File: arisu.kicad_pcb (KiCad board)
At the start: 2 copper layers, 339.1 x 118.7 mm, 166 parts, among them J1 USB_B_Micro, J10 PF6, J11 PF7, J12 VCC, J13 D+, J14 D-, J15 GND, J2 MISO, J3 VCC, J4 SCK, J5 MOSI, J6 RES, J7 GND, J8 PF4, J9 PF5, SW1 SW_Push, SW10 SW_Push, SW11 SW_Push, SW12 SW_Push, SW13 SW_Push, SW14 SW_Push, SW15 SW_Push, SW16 SW_Push, SW17 SW_Push, SW18 SW_Push, SW19 SW_Push, SW2 SW_Push, SW20 SW_Push, SW21 SW_Push, SW22 SW_Push, SW23 SW_Push, SW24 SW_Push, SW25 SW_Push, SW26 SW_Push, SW27 SW_Push, SW28 SW_Push, SW29 SW_Push, SW3 SW_Push, SW30 SW_Push, SW31 SW_Push, SW32 SW_Push, SW33 SW_Push, SW34 SW_Push, SW35 SW_Push, SW36 SW_Push, SW37 SW_Push, SW38 SW_Push, SW39 SW_Push, SW4 SW_Push, SW40 SW_Push, SW41 SW_Push, SW42 SW_Push, SW43 SW_Push, SW44 SW_Push, SW45 SW_Push, SW46 SW_Push, SW47 SW_Push, SW48 SW_Push, SW49 SW_Push, SW5 SW_Push, SW50 SW_Push, SW51 SW_Push, SW52 SW_Push, SW53 SW_Push, SW54 SW_Push, SW55 SW_Push, SW56 SW_Push, SW57 SW_Push, SW58 SW_Push, SW59 SW_Push, SW6 SW_Push, SW60 SW_Push, SW61 SW_Push, SW62 SW_Push, SW63 SW_Push, SW64 SW_Push, SW65 SW_Push, SW66 SW_Push, SW67 SW_Push, SW7 SW_Push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

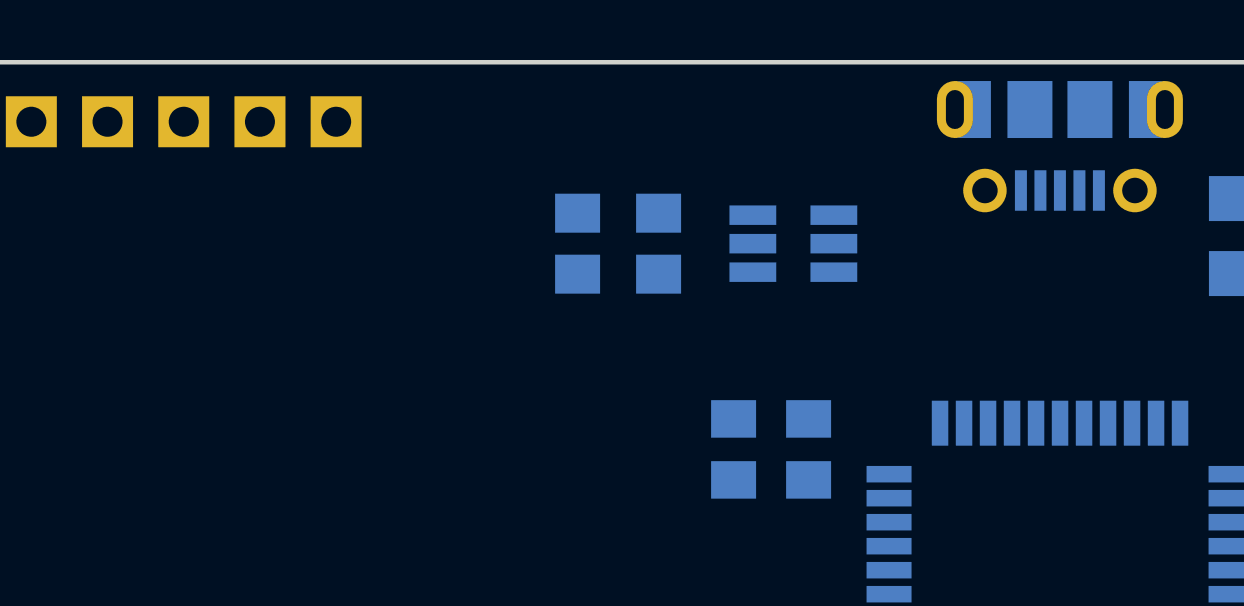
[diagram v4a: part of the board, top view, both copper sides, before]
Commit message: Route differential pair D+/D- pins to MCU
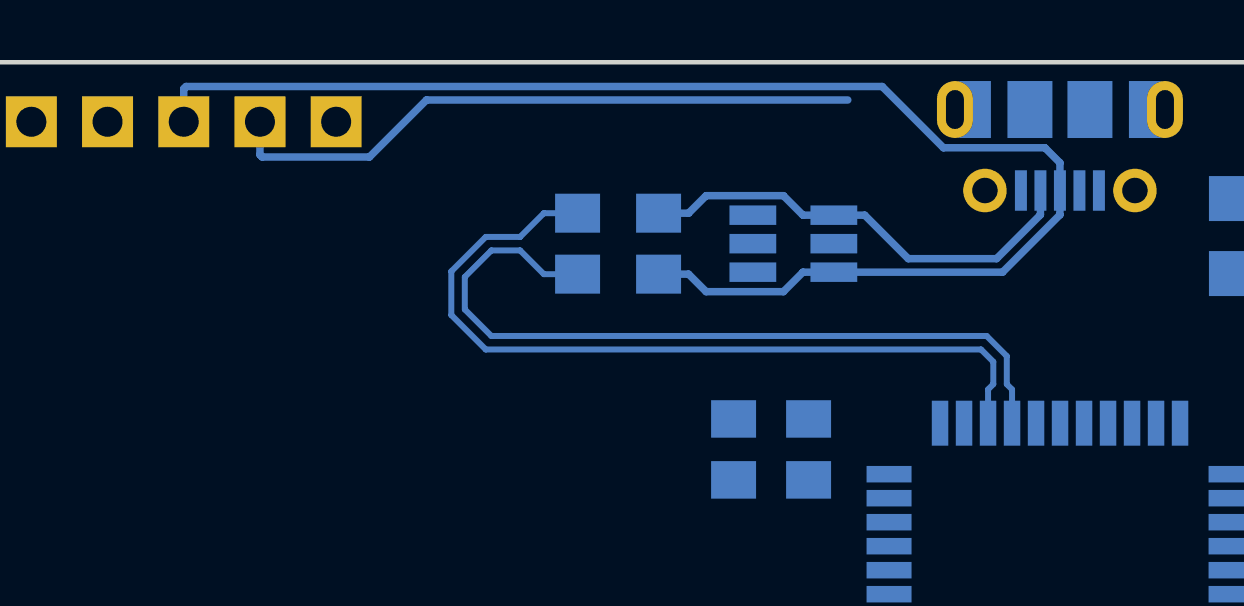
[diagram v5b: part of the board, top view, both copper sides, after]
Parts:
- moved R1 2.03 mm to (160.8, 31.5)
- moved R2 2.03 mm to (160.8, 29.5)
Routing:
- net Net-(J1-Pad3): track 0.00 -> 47.8 mm
- net Net-(J1-Pad2): track 0.00 -> 36.8 mm
- net D-: track 0.00 -> 27.3 mm
- net D+: track 0.00 -> 26.6 mm
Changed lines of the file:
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@@
     (thickness 1.6)
     (drawings 1380)
-    (tracks 0)
+    (tracks 52)
     (zones 0)
     (modules 166)
@@
   )
   (module Resistors_SMD:R_0805_HandSoldering (layer B.Cu)
-    (at 160.782 29.464)
+    (at 160.782 31.496)
     (descr "Resistor SMD 0805, hand soldering")
     (tags "resistor 0805")
@@
   )
   (module Resistors_SMD:R_0805_HandSoldering (layer B.Cu)
-    (at 160.782 31.496)
+    (at 160.782 29.464)
     (descr "Resistor SMD 0805, hand soldering")
     (tags "resistor 0805")
@@
   (gr_line (start 40.34 32.02) (end 40.64 31.72) (layer Eco2.User) (width 0.2))
   (gr_line (start 40.64 45.72) (end 40.34 45.42) (layer Eco2.User) (width 0.2))
+  (segment (start 175.509855 29.518002) (end 175.509855 28.708) (width 0.25) (layer B.Cu) (net 78))
+  (segment (start 167.974 31.43) (end 173.597857 31.43) (width 0.25) (layer B.Cu) (net 78))
+  (segment (start 173.597857 31.43) (end 175.509855 29.518002) (width 0.25) (layer B.Cu) (net 78))
+  (segment (start 166.944 31.43) (end 167.974 31.43) (width 0.25) (layer B.Cu) (net 78))
+  (segment (start 166.293999 32.080001) (end 166.944 31.43) (width 0.25) (layer B.Cu) (net 78))
+  (segment (start 163.716001 32.080001) (end 166.293999 32.080001) (width 0.25) (layer B.Cu) (net 78))
+  (segment (start 163.132 31.496) (end 163.716001 32.080001) (width 0.25) (layer B.Cu) (net 78))
+  (segment (start 162.132 31.496) (end 163.132 31.496) (width 0.25) (layer B.Cu) (net 78))
+  (segment (start 175.009865 27.28301) (end 175.509855 27.783) (width 0.25) (layer B.Cu) (net 78))
+  (segment (start 171.626704 27.28301) (end 175.009865 27.28301) (width 0.25) (layer B.Cu) (net 78))
+  (segment (start 175.509855 27.783) (end 175.509855 28.708) (width 0.25) (layer B.Cu) (net 78))
+  (segment (start 169.584693 25.240999) (end 171.626704 27.28301) (width 0.25) (layer B.Cu) (net 78))
+  (segment (start 146.379001 25.240999) (end 169.584693 25.240999) (width 0.25) (layer B.Cu) (net 78))
+  (segment (start 146.304 25.316) (end 146.379001 25.240999) (width 0.25) (layer B.Cu) (net 78))
+  (segment (start 146.304 26.416) (end 146.304 25.316) (width 0.25) (layer B.Cu) (net 78))
+  (segment (start 169.004 29.53) (end 167.974 29.53) (width 0.25) (layer B.Cu) (net 80) (status 1000000))
+  (segment (start 174.859855 28.708) (end 174.859855 29.518002) (width 0.25) (layer B.Cu) (net 80) (status 1000000))
+  (segment (start 174.859855 29.518002) (end 173.397867 30.97999) (width 0.25) (layer B.Cu) (net 80) (status 1000000))
+  (segment (start 173.397867 30.97999) (end 170.45399 30.97999) (width 0.25) (layer B.Cu) (net 80) (status 1000000))
+  (segment (start 170.45399 30.97999) (end 169.004 29.53) (width 0.25) (layer B.Cu) (net 80) (status 1000000))
+  (segment (start 166.944 29.53) (end 167.974 29.53) (width 0.25) (layer B.Cu) (net 80))
+  (segment (start 166.293999 28.879999) (end 166.944 29.53) (width 0.25) (layer B.Cu) (net 80))
+  (segment (start 163.716001 28.879999) (end 166.293999 28.879999) (width 0.25) (layer B.Cu) (net 80))
+  (segment (start 163.132 29.464) (end 163.716001 28.879999) (width 0.25) (layer B.Cu) (net 80))
+  (segment (start 162.132 29.464) (end 163.132 29.464) (width 0.25) (layer B.Cu) (net 80))
+  (segment (start 148.844 27.516) (end 148.919001 27.591001) (width 0.25) (layer B.Cu) (net 80))
+  (segment (start 148.844 26.416) (end 148.844 27.516) (width 0.25) (layer B.Cu) (net 80))
+  (segment (start 148.919001 27.591001) (end 152.494001 27.591001) (width 0.25) (layer B.Cu) (net 80))
+  (segment (start 152.494001 27.591001) (end 154.393993 25.691009) (width 0.25) (layer B.Cu) (net 80))
+  (segment (start 154.393993 25.691009) (end 168.438862 25.691009) (width 0.25) (layer B.Cu) (net 80))
+  (segment (start 173.739 35.163999) (end 173.739 34.2288) (width 0.2) (layer B.Cu) (net 89))
+  (segment (start 173.914 35.338999) (end 173.739 35.163999) (width 0.2) (layer B.Cu) (net 89))
+  (segment (start 173.914 36.464) (end 173.914 35.338999) (width 0.2) (layer B.Cu) (net 89))
+  (segment (start 173.739 34.2288) (end 173.0672 33.557) (width 0.2) (layer B.Cu) (net 89))
+  (segment (start 173.0672 33.557) (end 156.5572 33.557) (width 0.2) (layer B.Cu) (net 89))
+  (segment (start 156.5572 33.557) (end 155.673 32.6728) (width 0.2) (layer B.Cu) (net 89))
+  (segment (start 155.673 32.6728) (end 155.673 31.5892) (width 0.2) (layer B.Cu) (net 89))
+  (segment (start 158.306999 31.496) (end 159.432 31.496) (width 0.2) (layer B.Cu) (net 89))
+  (segment (start 157.515999 30.705) (end 158.306999 31.496) (width 0.2) (layer B.Cu) (net 89))
+  (segment (start 155.673 31.5892) (end 156.5572 30.705) (width 0.2) (layer B.Cu) (net 89))
+  (segment (start 156.5572 30.705) (end 157.515999 30.705) (width 0.2) (layer B.Cu) (net 89))
+  (segment (start 173.289 35.163999) (end 173.289 34.4152) (width 0.2) (layer B.Cu) (net 90))
+  (segment (start 173.114 36.464) (end 173.114 35.338999) (width 0.2) (layer B.Cu) (net 90))
+  (segment (start 173.114 35.338999) (end 173.289 35.163999) (width 0.2) (layer B.Cu) (net 90))
+  (segment (start 173.289 34.4152) (end 172.8808 34.007) (width 0.2) (layer B.Cu) (net 90))
+  (segment (start 172.8808 34.007) (end 156.3708 34.007) (width 0.2) (layer B.Cu) (net 90))
+  (segment (start 156.3708 34.007) (end 155.223 32.8592) (width 0.2) (layer B.Cu) (net 90))
+  (segment (start 155.223 32.8592) (end 155.223 31.4028) (width 0.2) (layer B.Cu) (net 90))
+  (segment (start 156.3708 30.255) (end 157.515999 30.255) (width 0.2) (layer B.Cu) (net 90))
+  (segment (start 155.223 31.4028) (end 156.3708 30.255) (width 0.2) (layer B.Cu) (net 90))
+  (segment (start 157.515999 30.255) (end 158.306999 29.464) (width 0.2) (layer B.Cu) (net 90))
+  (segment (start 158.306999 29.464) (end 159.432 29.464) (width 0.2) (layer B.Cu) (net 90))
 )

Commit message: Route all components
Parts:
- renumbered J13 to D+, J14 to D-, J7 to GND, J15 to GND, J2 to MISO, J5 to MOSI, J8 to PF4, J9 to PF5, J10 to PF6, J11 to PF7, J6 to RES, J4 to SCK, J3 to VCC, J12 to VCC
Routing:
- net /row4: track 0.00 -> 433.8 mm, vias 0 -> 2
- net /row3: track 0.00 -> 432.5 mm, vias 0 -> 2
- net /row2: track 0.00 -> 399.4 mm, vias 0 -> 4
- net /row1: track 0.00 -> 383.4 mm, vias 0 -> 4
- net /row0: track 0.00 -> 328.0 mm, vias 0 -> 4
- net /MISO: track 0.00 -> 272.2 mm, vias 0 -> 1
- net /col13: track 0.00 -> 269.0 mm
- net /col12: track 0.00 -> 249.0 mm
- net /col11: track 0.00 -> 224.6 mm
- net /col10: track 0.00 -> 221.3 mm
- net /col0: track 0.00 -> 204.4 mm
- net VCC: track 0.00 -> 200.5 mm, vias 0 -> 9
- net /col2: track 0.00 -> 175.7 mm, vias 0 -> 2
- net /col1: track 0.00 -> 166.8 mm
- net /SCK: track 0.00 -> 157.0 mm, vias 0 -> 2
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- added copper zone on F.Cu, net GND

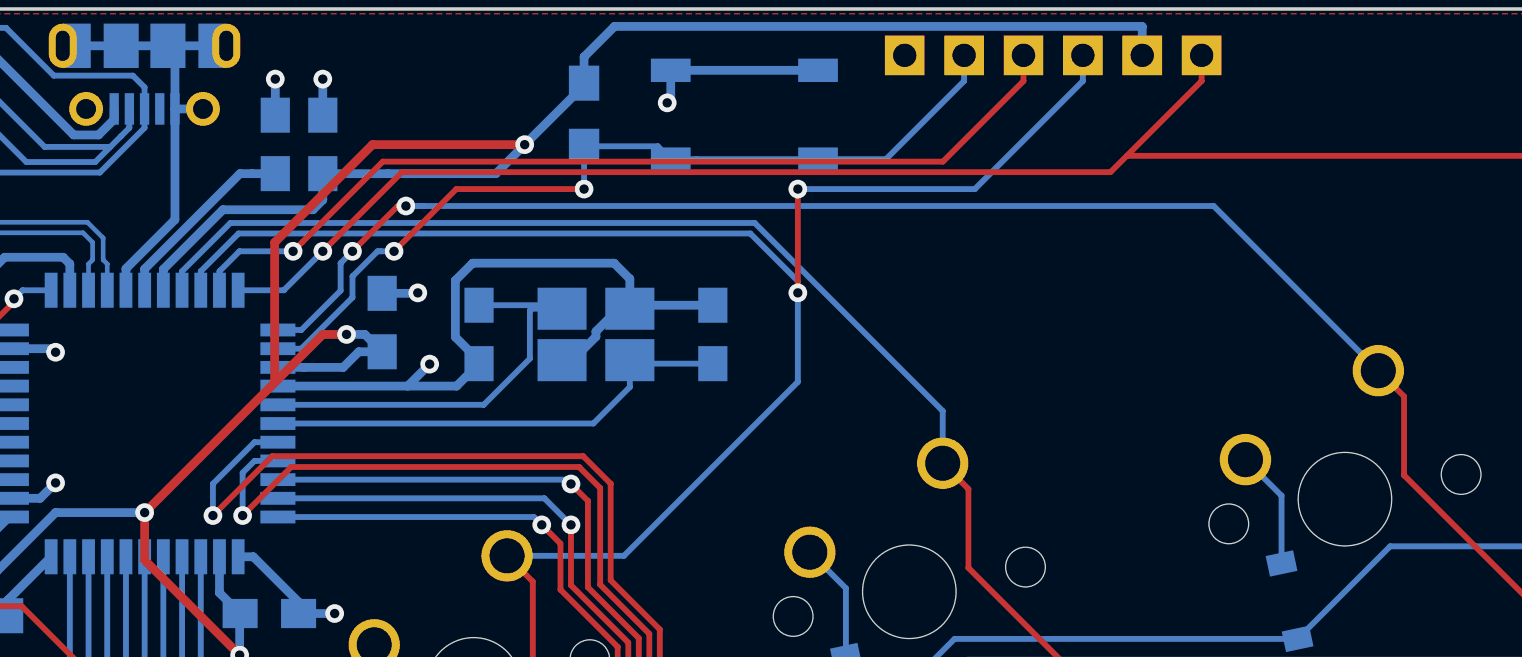
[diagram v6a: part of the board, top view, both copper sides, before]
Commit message: Optimize crystal placement
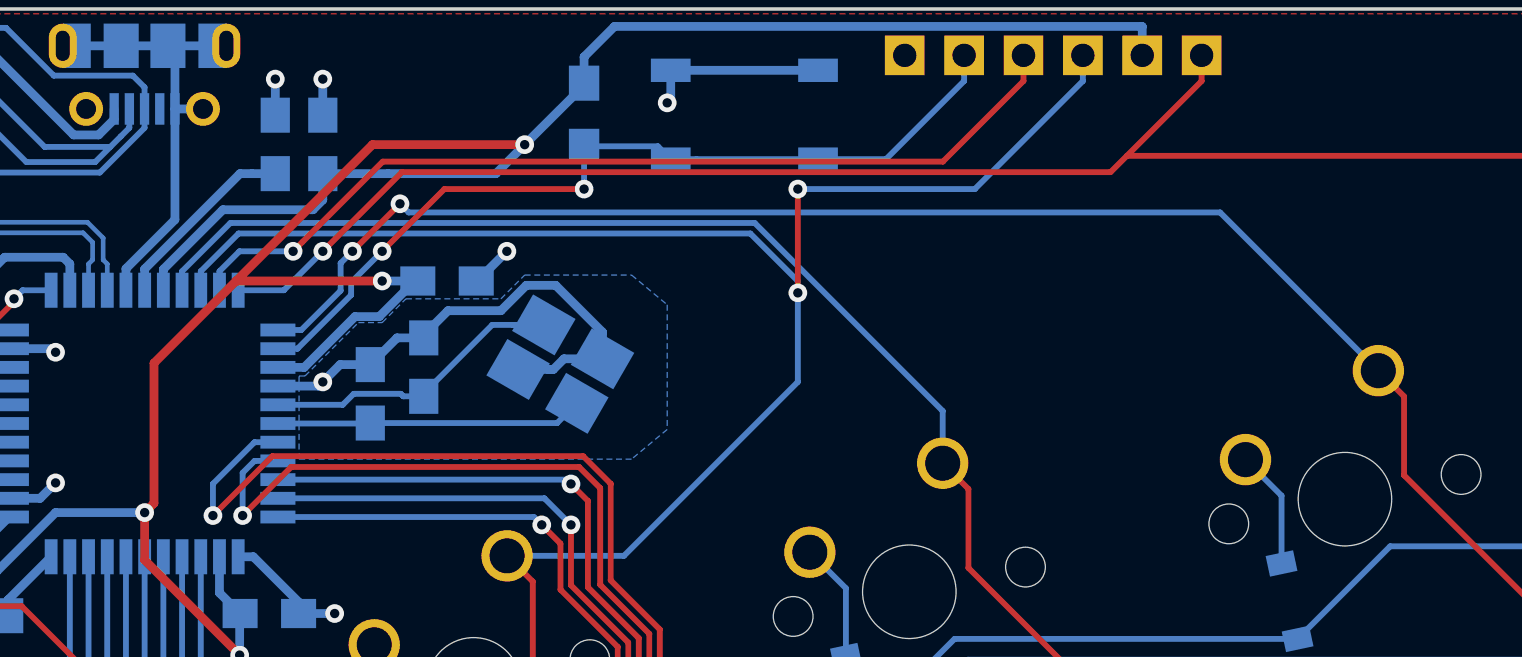
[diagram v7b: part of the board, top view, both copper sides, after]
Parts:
- moved C1 14.9 mm to (185.2, 40.9)
- moved C9 3.29 mm to (188.4, 36.1), turned to 0 degrees
- moved C2 2.75 mm to (187.5, 39.8), turned to 90 degrees
- moved Y1 1.98 mm to (193.3, 39.6), turned to 150 degrees
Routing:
- net GND: track 81.2 -> 71.2 mm
- net XTAL1: track 20.5 -> 13.1 mm
- net XTAL2: track 18.7 -> 13.0 mm
- net VCC: track 200.5 -> 205.4 mm
- added copper zone on B.Cu, net GND
